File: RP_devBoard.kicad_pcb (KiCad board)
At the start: 2 copper layers, 19 parts, among them J1 Conn_01x04, J2 Conn_01x04, J3 TC2030, J4 TC2030, J6 USB_C_Receptacle, U2 ESP32-C3-WROOM-02, U3 BME280, U4 NCP1117-3.3_SOT223

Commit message: Adding source, source control
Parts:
- removed the U1 at (132.2, 71.4)
- removed the U1 at (146.5, 80.8)
- added C10: 100nF, Capacitor_SMD:C_0402_1005Metric, F.Cu at (118.1, 78.4)
- added C11: 100nF, Capacitor_SMD:C_0402_1005Metric, F.Cu at (118.1, 80.4)
- added C12: 100nF, Capacitor_SMD:C_0402_1005Metric, F.Cu at (118.1, 82.4)
- added C13: 100nF, Capacitor_SMD:C_0402_1005Metric, F.Cu at (118.1, 84.3)
- added C14: 100nF, Capacitor_SMD:C_0402_1005Metric, F.Cu at (118.1, 86.3)
- added C15: 100nF, Capacitor_SMD:C_0402_1005Metric, F.Cu at (118.1, 88.3)
- added C16: 100nF, Capacitor_SMD:C_0402_1005Metric, F.Cu at (118.1, 90.3)
- added C17: 100nF, Capacitor_SMD:C_0402_1005Metric, F.Cu at (121.0, 78.4)
- added C18: 15pF, Capacitor_SMD:C_0402_1005Metric, F.Cu at (121.0, 80.4)
- added C19: 15pF, Capacitor_SMD:C_0402_1005Metric, F.Cu at (121.0, 82.4)
- added C20: 100nF, Capacitor_SMD:C_0402_1005Metric, F.Cu at (121.0, 84.3)
- added C21: 100nF, Capacitor_SMD:C_0402_1005Metric, F.Cu at (121.0, 86.3)
- added C22: 100nF, Capacitor_SMD:C_0402_1005Metric, F.Cu at (96.2, 78.8)
- added C23: 100nF, Capacitor_SMD:C_0402_1005Metric, F.Cu at (96.2, 80.8)
- added C24: 100nF, Capacitor_SMD:C_0402_1005Metric, F.Cu at (99.6, 45.2)
- added C25: 1uF, Capacitor_SMD:C_0603_1608Metric, F.Cu at (100.2, 37.9)
- added C26: 10uF, Capacitor_SMD:C_0603_1608Metric, F.Cu at (100.2, 40.4)
- added C27: 100nF, Capacitor_SMD:C_0402_1005Metric, F.Cu at (96.2, 82.8)
- added C28: 100nF, Capacitor_SMD:C_0402_1005Metric, F.Cu at (96.2, 84.8)
- added C29: 10uF, Capacitor_SMD:C_0603_1608Metric, F.Cu at (106.2, 42.9)
- added C30: 10uF, Capacitor_SMD:C_0603_1608Metric, F.Cu at (106.2, 45.4)
- added C5: 100nF, Capacitor_SMD:C_0402_1005Metric, F.Cu at (115.3, 82.4)
- added C7: 100nF, Capacitor_SMD:C_0402_1005Metric, F.Cu at (115.3, 86.3)
- added C8: 4.7uF, Capacitor_SMD:C_0402_1005Metric, F.Cu at (115.3, 88.3)
- added C9: 100nF, Capacitor_SMD:C_0402_1005Metric, F.Cu at (115.3, 90.3)
- added D1: SD1206S040S2R0, Diode_SMD:D_1206_3216Metric, F.Cu at (97.6, 87.4)
- added D2: SD1206S040S2R0, Diode_SMD:D_1206_3216Metric, F.Cu at (97.6, 90.8)
- added J5: USB_C_Receptacle, Connector_USB:USB_C_Receptacle_Amphenol_12401610E4-2A, F.Cu at (83.7, 71.6)
- added L2: 680nF, sadman_power_passive:L_1212_3030Metric, F.Cu at (110.3, 38.7)
- added R10: 0, Resistor_SMD:R_0603_1608Metric, F.Cu at (122.7, 73.5)
- added R11: 5.1k, Resistor_SMD:R_0603_1608Metric, F.Cu at (75.8, 71.5)
- added R12: 5.1k, Resistor_SMD:R_0603_1608Metric, F.Cu at (75.8, 74.0)
- added R13: 10k, Resistor_SMD:R_0603_1608Metric, F.Cu at (100.2, 42.9)
- added R14: 10k, Resistor_SMD:R_0603_1608Metric, F.Cu at (75.8, 76.5)
- added R15: 10k, Resistor_SMD:R_0603_1608Metric, F.Cu at (75.8, 79.0)
- added R16: 10k, Resistor_SMD:R_0603_1608Metric, F.Cu at (75.8, 81.5)
- added R4: 27, Resistor_SMD:R_0402_1005Metric, F.Cu at (123.9, 80.4)
- added R5: 27, Resistor_SMD:R_0402_1005Metric, F.Cu at (123.9, 82.4)
- added R6: 1K, Resistor_SMD:R_0402_1005Metric, F.Cu at (123.9, 84.4)
- added R7: 1K, Resistor_SMD:R_0402_1005Metric, F.Cu at (123.9, 86.4)
- added R8: 1K, Resistor_SMD:R_0402_1005Metric, F.Cu at (123.9, 88.4)
- added R9: 0, Resistor_SMD:R_0603_1608Metric, F.Cu at (122.7, 71.0)
- added U1: RP2350B, Package_DFN_QFN:QFN-80-1EP_10x10mm_P0.4mm_EP3.4x3.4mm, F.Cu at (110.0, 71.3)
- added U10: USBLC6-2SC6, Package_TO_SOT_SMD:SOT-23-6, F.Cu at (71.2, 81.5)
- added U11: USBLC6-2SC6, Package_TO_SOT_SMD:SOT-23-6, F.Cu at (71.2, 86.1)
- added U12: TPS628502, Package_TO_SOT_SMD:SOT-583-8, F.Cu at (110.1, 42.8)
- added U5: W25Q128JVS, Package_SO:SOIC-8_5.3x5.3mm_P1.27mm, F.Cu at (108.7, 81.0)
- added U6: W25Q128JVS, Package_SO:SOIC-8_5.3x5.3mm_P1.27mm, F.Cu at (108.7, 87.9)
- added U7: MAX40200AUK, Package_TO_SOT_SMD:SOT-23-5, F.Cu at (71.2, 67.6)
- added U8: MAX40200AUK, Package_TO_SOT_SMD:SOT-23-5, F.Cu at (71.2, 72.2)
- added U9: MAX40200AUK, Package_TO_SOT_SMD:SOT-23-5, F.Cu at (71.2, 76.9)
- added Y1: 12MHz, Crystal:Crystal_SMD_3225-4Pin_3.2x2.5mm, F.Cu at (118.7, 67.5)
- U4: value NCP1117-3.3_SOT223 -> TPS62932; footprint Package_TO_SOT_SMD:SOT-223-3_TabPin2 -> Package_TO_SOT_SMD:SOT-583-8
- moved J2 132.4 mm to (82.2, 87.2)
- moved J3 124.8 mm to (90.7, 80.4)
- moved J4 124.8 mm to (90.7, 85.4)
- moved U3 100.6 mm to (116.6, 38.9)
- moved U2 97.0 mm to (83.4, 55.5)
- moved J1 82.8 mm to (82.2, 81.0)
- moved R1 69.4 mm to (75.8, 66.5)
- moved R2 69.4 mm to (75.8, 69.0)
- moved U4 45.4 mm to (99.4, 79.9), turned to 0 degrees
- moved C6 28.3 mm to (115.3, 84.3)
- moved C3 27.4 mm to (115.3, 78.4)
- moved C4 27.4 mm to (115.3, 80.4)
- moved C1 23.1 mm to (106.2, 37.9), turned to 0 degrees
- moved J6 20.1 mm to (95.6, 71.6), turned to 0 degrees
- moved C2 16.2 mm to (106.2, 40.4), turned to 0 degrees
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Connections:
- net /RP2350B/1V1 renamed +1V1
- net /USB_DN renamed /COM_PORTS/USB0_DN
- net /USB_DP renamed /COM_PORTS/USB0_DP
- C1 pad 1: Net-(U4-VI) -> /COM_PORTS/BUCK/VIN
- C2 pad 1: +3V3 -> /COM_PORTS/BUCK/VOUT_3V3
- C4 pad 1: /RP2350B/3V3 -> +3V3
- J1 pad 1: unconnected-(J1-Pin_1-Pad1) -> GND
- J1 pad 2: unconnected-(J1-Pin_2-Pad2) -> +3V3_QWIIC
- J1 pad 3: unconnected-(J1-Pin_3-Pad3) -> /COM_PORTS/RP_SDA
- J1 pad 4: unconnected-(J1-Pin_4-Pad4) -> /COM_PORTS/RP_CLK
- J2 pad 1: unconnected-(J2-Pin_1-Pad1) -> GND
- J2 pad 2: unconnected-(J2-Pin_2-Pad2) -> +3V3_QWIIC
- J2 pad 3: unconnected-(J2-Pin_3-Pad3) -> /COM_PORTS/RP_SDA
- J2 pad 4: unconnected-(J2-Pin_4-Pad4) -> /COM_PORTS/RP_CLK
- J3 pad 1: unconnected-(J3-Pad1) -> +3V3_TC1
- J3 pad 2: unconnected-(J3-Pad2) -> /COM_PORTS/RP_SWD
- J3 pad 3: unconnected-(J3-Pad3) -> /COM_PORTS/RP_NRESET
- J3 pad 4: unconnected-(J3-Pad4) -> /COM_PORTS/RP_SWCLK
- J3 pad 5: unconnected-(J3-Pad5) -> GND
- J3 pad 6: unconnected-(J3-Pad6) -> /COM_PORTS/RP_SWO
- J4 pad 1: unconnected-(J4-Pad1) -> +3V3_TC2
- J4 pad 2: unconnected-(J4-Pad2) -> /COM_PORTS/ESP_TX
- J4 pad 3: unconnected-(J4-Pad3) -> /COM_PORTS/ESP_TX
- J4 pad 4: unconnected-(J4-Pad4) -> GND
- J4 pad 5: unconnected-(J4-Pad5) -> /COM_PORTS/ESP_BOOT
- J4 pad 6: unconnected-(J4-Pad6) -> /COM_PORTS/RP_NRESET
- J6 pad A4: Net-(U4-VI) -> VUSB0
- J6 pad A9: Net-(U4-VI) -> VUSB0
- J6 pad B4: Net-(U4-VI) -> VUSB0
- J6 pad B9: Net-(U4-VI) -> VUSB0
- R3 pad 1: /RP2350B/3V3 -> +3V3
- U2 pad 1: unconnected-(U2-3V3-Pad1) -> +3V3
- U2 pad 10: unconnected-(U2-IO10-Pad10) -> /ESP32/ESP_SS
- U2 pad 11: unconnected-(U2-IO20/RXD-Pad11) -> /ESP32/ESP_RX
- U2 pad 12: unconnected-(U2-IO21/TXD-Pad12) -> /ESP32/ESP_TX
- U2 pad 13: unconnected-(U2-IO18-Pad13) -> /USB1_DM
- U2 pad 14: unconnected-(U2-IO19-Pad14) -> /USB1_DP
- U2 pad 16: unconnected-(U2-IO2-Pad16) -> /ESP32/ESP_MISO
- U2 pad 18: unconnected-(U2-IO0-Pad18) -> /ESP32/ESP_BOOT
- U2 pad 19: Net-(U2-GND-Pad19) -> GND
- U2 pad 2: unconnected-(U2-EN-Pad2) -> /ESP32/ESP_RESET
- U2 pad 5: unconnected-(U2-IO6-Pad5) -> /ESP32/ESP_CLK
- U2 pad 6: unconnected-(U2-IO7-Pad6) -> /ESP32/ESP_MOSI
- U2 pad 9: Net-(U2-GND-Pad19) -> GND
- U4 pad 1: GND -> unconnected-(U4-RT-Pad1)
- U4 pad 2: +3V3 -> unconnected-(U4-EN-Pad2)
- U4 pad 3: Net-(U4-VI) -> unconnected-(U4-VIN-Pad3)

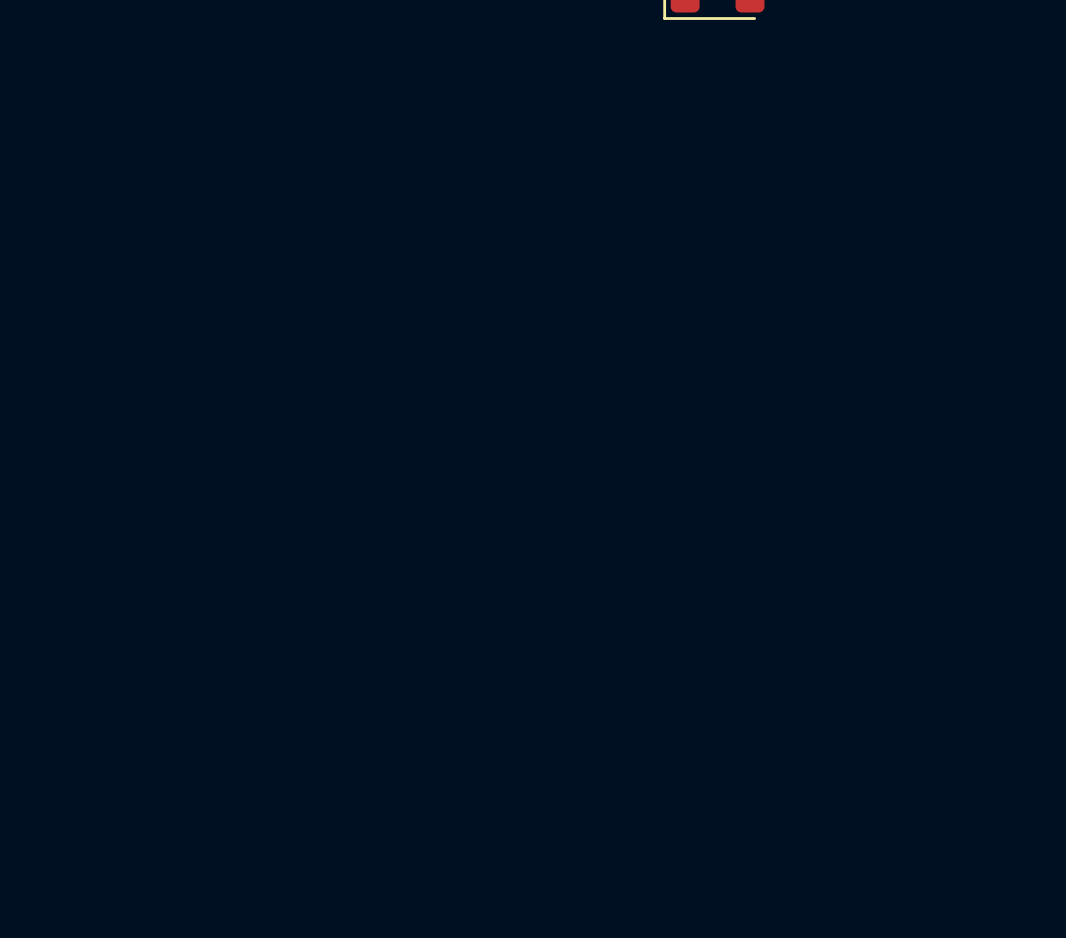
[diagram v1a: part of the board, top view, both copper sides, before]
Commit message: Adding mikroBUS
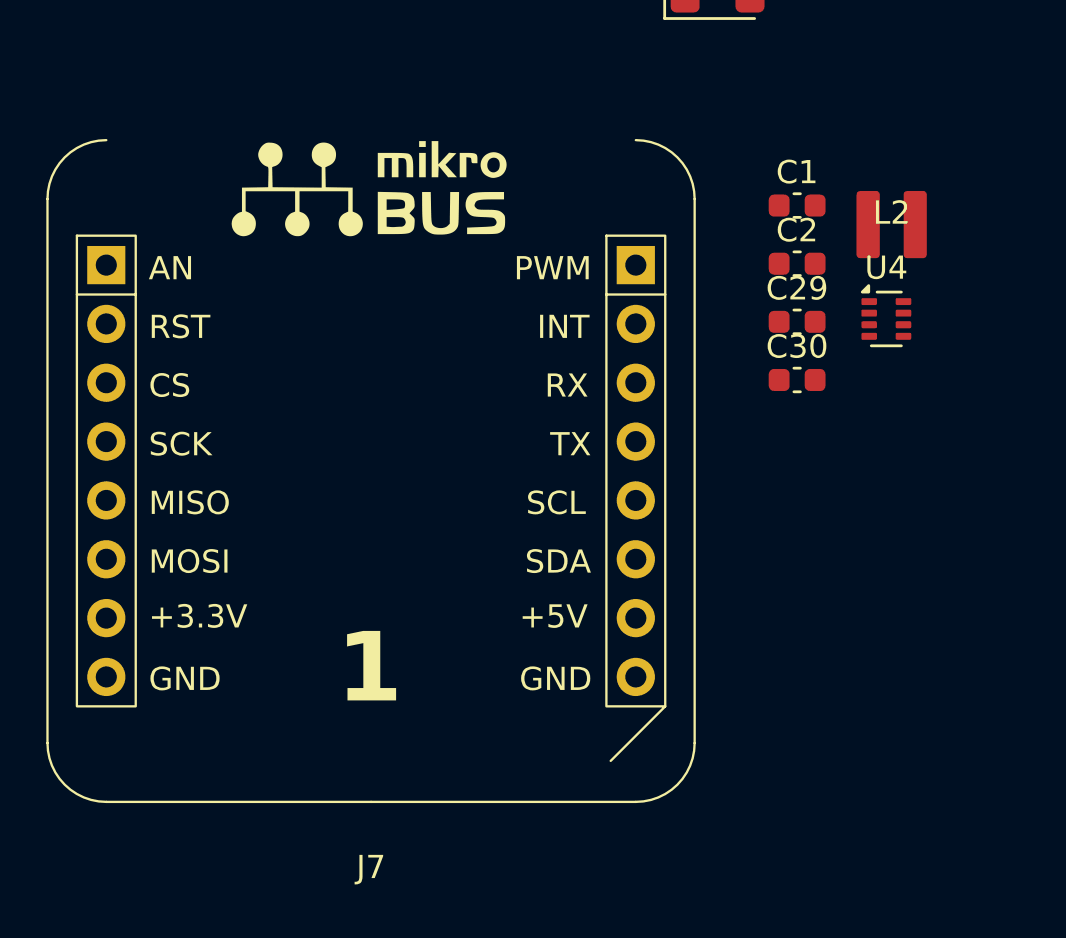
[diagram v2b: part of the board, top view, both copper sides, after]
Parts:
- added C1: 10uF, Capacitor_SMD:C_0603_1608Metric, F.Cu at (101.0, 100.0)
- added C2: 10uF, Capacitor_SMD:C_0603_1608Metric, F.Cu at (101.0, 102.5)
- added C29: 10uF, Capacitor_SMD:C_0603_1608Metric, F.Cu at (101.0, 105.0)
- added C30: 10uF, Capacitor_SMD:C_0603_1608Metric, F.Cu at (101.0, 107.6)
- added J7: Conn_02x08_Counter_Clockwise, Sadman_connectors:MikroBUS, F.Cu at (82.6, 102.6)
- added L2: 680nF, sadman_power_passive:L_1212_3030Metric, F.Cu at (105.1, 100.8)
- added U4: TPS628502, Package_TO_SOT_SMD:SOT-583-8, F.Cu at (104.8, 104.9)
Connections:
- net /COM_PORTS/RP_CLK renamed /RP_CLK
- net /COM_PORTS/RP_SDA renamed /RP_SDA
- net /COM_PORTS/RP_SWO renamed /RP_SWO
- C23 pad 2: +3V3_QWIIC -> +3V3
- J1 pad 2: +3V3_QWIIC -> +3V3
- J3 pad 2: /COM_PORTS/RP_SWD -> /RP_SWD
- J3 pad 4: /COM_PORTS/RP_SWCLK -> /RP_SWCLK
- J4 pad 3: /COM_PORTS/ESP_TX -> /COM_PORTS/ESP_RX
- J4 pad 6: /COM_PORTS/RP_NRESET -> /COM_PORTS/ESP_EN
- R16 pad 2: +3V3_QWIIC -> +3V3_USB
- R4 pad 2: /USB_DP -> /RP_USB_DP
- R5 pad 2: /USB_DN -> /RP_USB_DN
- U1 pad 77: /ESP32/ESP_MOSI -> /RP2350B/RPB_SPI_MISO
- U1 pad 78: /ESP32/ESP_MISO -> /RP2350B/RPB_SPI_MOSI
- U1 pad 79: /ESP32/ESP_CLK -> /RP2350B/RPB_SPI_CLK
- U1 pad 80: /ESP32/ESP_SS -> /RP2350B/RPB_SPI_SS
- U10 pad 4: /COM_PORTS/USB0_DN_OUT -> /RP_USB_DN
- U10 pad 6: /COM_PORTS/USB0_DP_OUT -> /RP_USB_DP
- U11 pad 4: /COM_PORTS/USB1_DN_OUT -> /ESP_USB_DN
- U11 pad 6: /COM_PORTS/USB1_DP_OUT -> /ESP_USB_DP
- U2 pad 13: /USB1_DM -> /ESP_USB_DN
- U2 pad 14: /USB1_DP -> /ESP_USB_DP
- U7 pad 5: /COM_PORTS/3V3_SYSTEM -> +3V3
- U8 pad 5: /COM_PORTS/3V3_SYSTEM -> +3V3
- U9 pad 1: +3V3_QWIIC -> +3V3_USB
- U9 pad 5: /COM_PORTS/3V3_SYSTEM -> +3V3

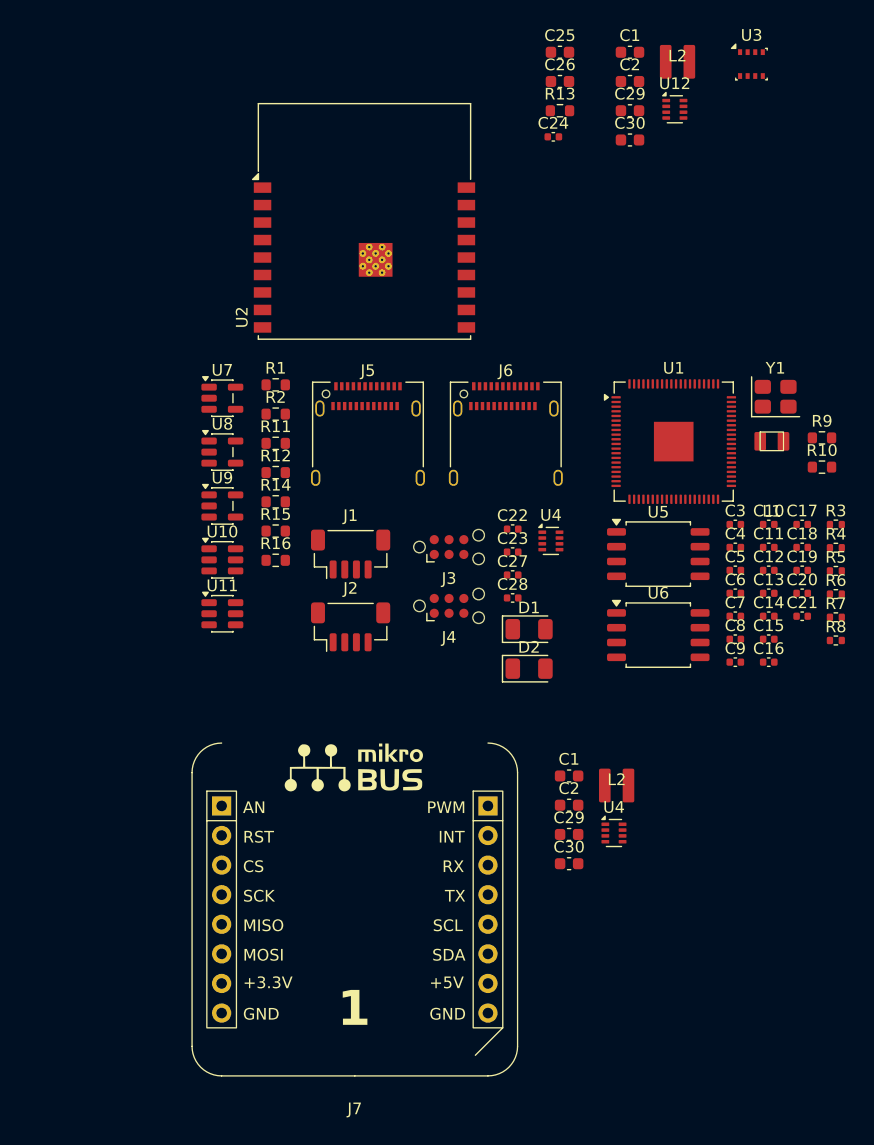
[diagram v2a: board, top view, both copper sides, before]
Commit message: Modificaciond de conexiones
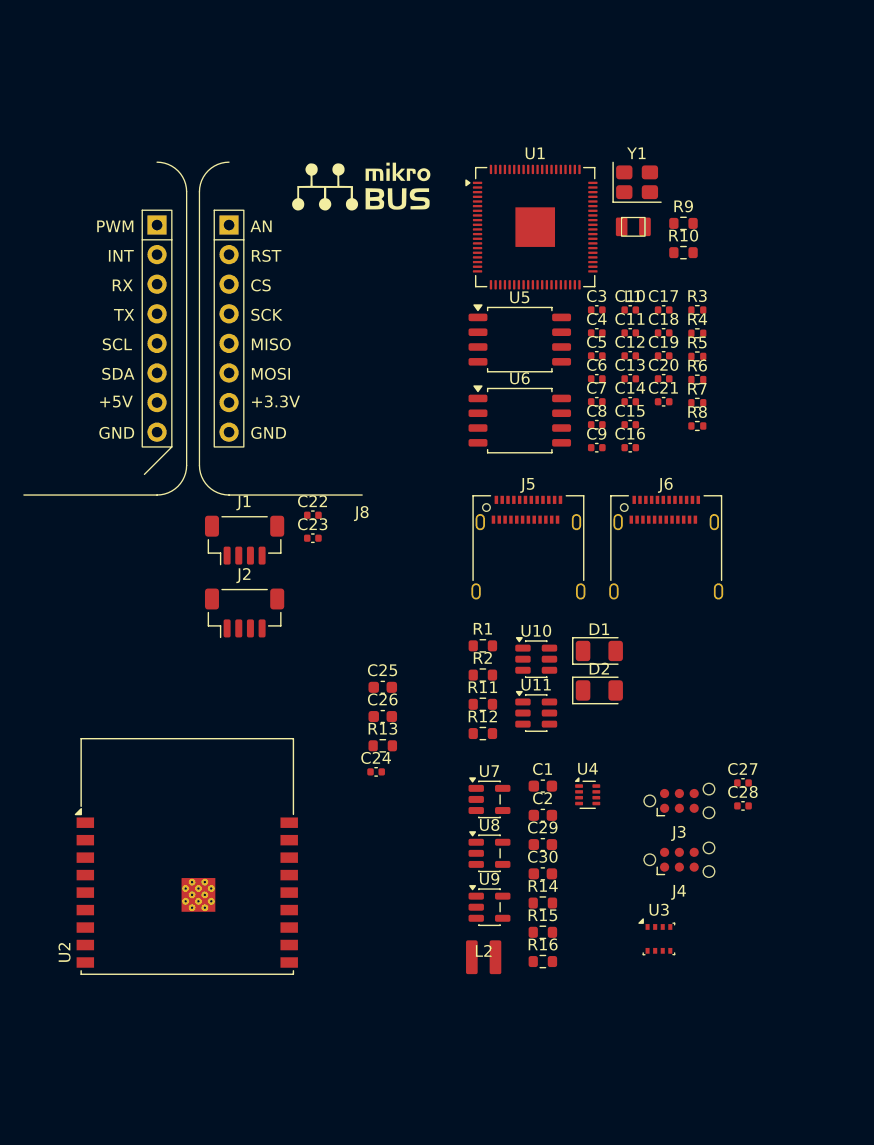
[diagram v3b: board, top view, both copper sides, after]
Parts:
- removed the C1 at (106.2, 37.9)
- removed the C1 at (101.0, 100.0)
- removed the C2 at (101.0, 102.5)
- removed the C2 at (106.2, 40.4)
- removed the C29 at (106.2, 42.9)
- removed the C29 at (101.0, 105.0)
- removed the C30 at (106.2, 45.4)
- removed the C30 at (101.0, 107.6)
- removed J7: Conn_02x08_Counter_Clockwise, Sadman_connectors:MikroBUS
- removed the L2 at (110.3, 38.7)
- removed the L2 at (105.1, 100.8)
- removed U12: TPS628502, Package_TO_SOT_SMD:SOT-583-8
- removed the U4 at (99.4, 79.9)
- removed the U4 at (104.8, 104.9)
- added C1: 10uF, Capacitor_SMD:C_0603_1608Metric, F.Cu at (98.7, 100.9)
- added C2: 10uF, Capacitor_SMD:C_0603_1608Metric, F.Cu at (98.7, 103.4)
- added C29: 10uF, Capacitor_SMD:C_0603_1608Metric, F.Cu at (98.7, 105.9)
- added C30: 10uF, Capacitor_SMD:C_0603_1608Metric, F.Cu at (98.7, 108.4)
- added J8: ~, Sadman_connectors:MikroBUS_Left, F.Cu at (83.2, 75.9)
- added J9: ~, Sadman_connectors:MikroBUS_Right, F.Cu at (54.2, 75.9)
- added L2: 680nF, sadman_power_passive:L_1212_3030Metric, F.Cu at (93.7, 115.6)
- added U4: TPS628502, Package_TO_SOT_SMD:SOT-583-8, F.Cu at (102.6, 101.6)
- moved U3 75.5 mm to (108.7, 114.0)
- moved C24 56.6 mm to (84.4, 99.7)
- moved C25 56.6 mm to (85.0, 92.4)
- moved C26 56.6 mm to (85.0, 94.9)
- moved U2 56.6 mm to (68.2, 110.0)
- moved R13 56.6 mm to (85.0, 97.4)
- moved R14 41.4 mm to (98.7, 110.9)
- moved R15 41.4 mm to (98.7, 113.5)
- moved R16 41.4 mm to (98.7, 116.0)
- moved U7 41.4 mm to (94.2, 102.0)
- moved U8 41.4 mm to (94.2, 106.7)
- moved U9 41.4 mm to (94.2, 111.3)
- moved J3 29.4 mm to (110.5, 102.2)
- moved J4 29.4 mm to (110.5, 107.2)
- moved R1 28.6 mm to (93.6, 88.9)
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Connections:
- net /COM_PORTS/USB0_DN renamed /USB_PORTS/USB0_DN
- net /COM_PORTS/USB0_DP renamed /USB_PORTS/USB0_DP
- net /COM_PORTS/USB1_DP renamed /USB_PORTS/USB1_DP
- net /ESP_USB_DN renamed /USB1_DM
- net /ESP_USB_DP renamed /USB1_DP
- net /RP2350B/RPB_SPI_MISO renamed /RP2350B/RPB_I2C_SDA
- net /RP2350B/RPB_SPI_MOSI renamed /RP2350B/RPB_I2C_SCL
- net /RP_SDA renamed /PERIPHERICS/RP_SDA
- net /RP_USB_DN renamed /USB0_DN
- net /RP_USB_DP renamed /USB0_DP
- net VIN renamed +5V
- C22 pad 2: +3V3_QWIIC -> +3V3
- C25 pad 1: /ESP32/ESP_RESET -> /ESP_EN
- J1 pad 4: /RP_CLK -> /PERIPHERICS/RP_CLK
- J2 pad 2: +3V3_QWIIC -> +3V3
- J2 pad 4: /RP_CLK -> /PERIPHERICS/RP_CLK
- J3 pad 3: /COM_PORTS/RP_NRESET -> /RP_NRESET
- J4 pad 2: /COM_PORTS/ESP_TX -> /ESP_TX
- J4 pad 3: /COM_PORTS/ESP_RX -> /ESP_RX
- J4 pad 5: /COM_PORTS/ESP_BOOT -> /ESP_BOOT
- J4 pad 6: /COM_PORTS/ESP_EN -> /ESP_EN
- J5 pad A7: /COM_PORTS/USB1_DM -> /USB_PORTS/USB1_DN
- J5 pad B7: /COM_PORTS/USB1_DM -> /USB_PORTS/USB1_DN
- R13 pad 1: /ESP32/ESP_RESET -> /ESP_EN
- U1 pad 1: unconnected-(U1-GPIO4-Pad1) -> /MK_RX
- U1 pad 2: unconnected-(U1-GPIO5-Pad2) -> /MK_TX
- U1 pad 23: unconnected-(U1-GPIO23-Pad23) -> /RP_SWO
- U1 pad 3: unconnected-(U1-GPIO6-Pad3) -> /MK_PWM
- U1 pad 35: /RP2350B/RP_NRESET -> /RP_NRESET
- U1 pad 4: unconnected-(U1-GPIO7-Pad4) -> /MK_INT
- U1 pad 44: unconnected-(U1-GPIO35-Pad44) -> /RP_MISO
- U1 pad 45: unconnected-(U1-GPIO36-Pad45) -> /RP_MOSI
- U1 pad 46: unconnected-(U1-GPIO37-Pad46) -> /RP_CLK
- U1 pad 47: unconnected-(U1-GPIO38-Pad47) -> /RP_SS0
- U1 pad 48: unconnected-(U1-GPIO39-Pad48) -> /RP_SS1
- U1 pad 49: unconnected-(U1-GPIO40_ADC0-Pad49) -> /MK_AIN
- U1 pad 6: unconnected-(U1-GPIO8-Pad6) -> /MK_RST
- U1 pad 79: /RP2350B/RPB_SPI_CLK -> unconnected-(U1-GPIO2-Pad79)
- U1 pad 80: /RP2350B/RPB_SPI_SS -> unconnected-(U1-GPIO3-Pad80)
- U11 pad 3: /COM_PORTS/USB1_DN -> /USB_PORTS/USB1_DN
- U2 pad 10: /ESP32/ESP_SS -> /RP_SS0
- U2 pad 11: /ESP32/ESP_RX -> /ESP_RX
- U2 pad 12: /ESP32/ESP_TX -> /ESP_TX
- U2 pad 16: /ESP32/ESP_MISO -> /RP_MISO
- U2 pad 18: /ESP32/ESP_BOOT -> /ESP_BOOT
- U2 pad 2: /ESP32/ESP_RESET -> /ESP_EN
- U2 pad 5: /ESP32/ESP_CLK -> /RP_CLK
- U2 pad 6: /ESP32/ESP_MOSI -> /RP_MOSI
